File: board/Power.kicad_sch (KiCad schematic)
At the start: 9 parts

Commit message: Adjusted diode footprints and grouped layout components
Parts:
- C4, C6, C7, C9: footprint BoCoFootprintLibrary:U1-Z_NCH -> Capacitor_THT:CP_Radial_D12.5mm_P5.00mm
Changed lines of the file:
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@@
 			)
 		)
-		(property "Footprint" "BoCoFootprintLibrary:U1-Z_NCH"
+		(property "Footprint" "Capacitor_THT:CP_Radial_D12.5mm_P5.00mm"
 			(at 63.5 34.29 0)
 			(effects
@@
 			)
 		)
-		(property "Footprint" "BoCoFootprintLibrary:U1-Z_NCH"
+		(property "Footprint" "Capacitor_THT:CP_Radial_D12.5mm_P5.00mm"
 			(at 74.93 34.29 0)
 			(effects
@@
 			)
 		)
-		(property "Footprint" "BoCoFootprintLibrary:U1-Z_NCH"
+		(property "Footprint" "Capacitor_THT:CP_Radial_D12.5mm_P5.00mm"
 			(at 40.64 34.29 0)
 			(effects
@@
 			)
 		)
-		(property "Footprint" "BoCoFootprintLibrary:U1-Z_NCH"
+		(property "Footprint" "Capacitor_THT:CP_Radial_D12.5mm_P5.00mm"
 			(at 52.07 34.29 0)
 			(effects

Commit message: Tentatively finished rev1.
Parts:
- C4, C6, C7, C9: footprint Capacitor_THT:CP_Radial_D12.5mm_P5.00mm -> Capacitor_THT:CP_Radial_D16.0mm_P7.50mm
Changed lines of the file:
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@@
 			)
 		)
-		(property "Footprint" "Capacitor_THT:CP_Radial_D12.5mm_P5.00mm"
+		(property "Footprint" "Capacitor_THT:CP_Radial_D16.0mm_P7.50mm"
 			(at 63.5 34.29 0)
 			(effects
@@
 			)
 		)
-		(property "Footprint" "Capacitor_THT:CP_Radial_D12.5mm_P5.00mm"
+		(property "Footprint" "Capacitor_THT:CP_Radial_D16.0mm_P7.50mm"
 			(at 74.93 34.29 0)
 			(effects
@@
 			)
 		)
-		(property "Footprint" "Capacitor_THT:CP_Radial_D12.5mm_P5.00mm"
+		(property "Footprint" "Capacitor_THT:CP_Radial_D16.0mm_P7.50mm"
 			(at 40.64 34.29 0)
 			(effects
@@
 			)
 		)
-		(property "Footprint" "Capacitor_THT:CP_Radial_D12.5mm_P5.00mm"
+		(property "Footprint" "Capacitor_THT:CP_Radial_D16.0mm_P7.50mm"
 			(at 52.07 34.29 0)
 			(effects

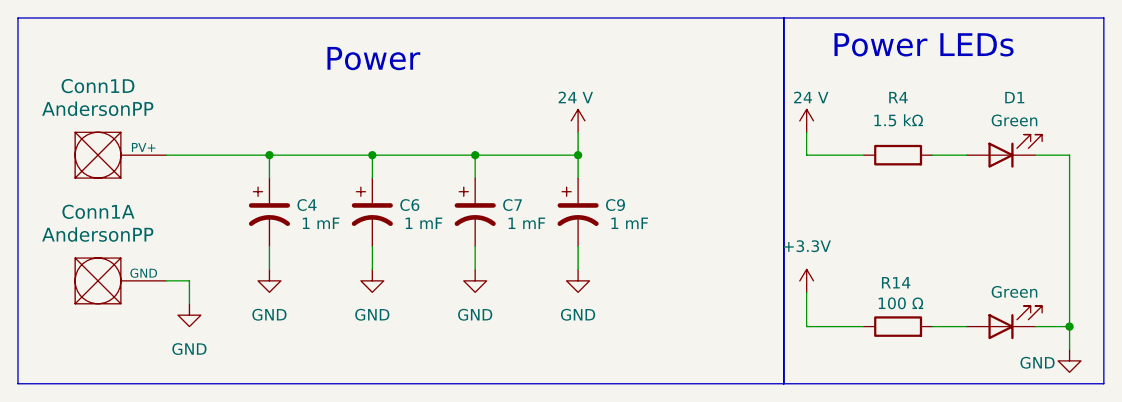
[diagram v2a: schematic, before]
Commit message: Fixed many issues found in Rev1 review prior to order
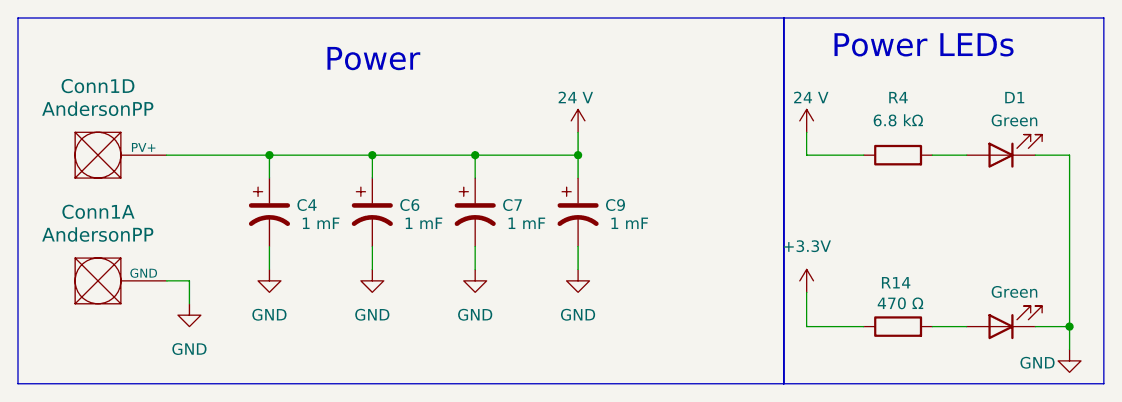
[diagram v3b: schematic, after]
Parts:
- R14: value 100 Ω -> 470 Ω
- R4: value 1.5 kΩ -> 6.8 kΩ
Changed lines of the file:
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@@
 			)
 		)
-		(property "Value" "1.5 kΩ"
+		(property "Value" "6.8 kΩ"
 			(at 110.49 24.13 90)
 			(effects
@@
 			)
 		)
-		(property "Value" "100 Ω"
+		(property "Value" "470 Ω"
 			(at 110.744 44.45 90)
 			(effects
